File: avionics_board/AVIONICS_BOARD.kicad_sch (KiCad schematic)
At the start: 4 parts

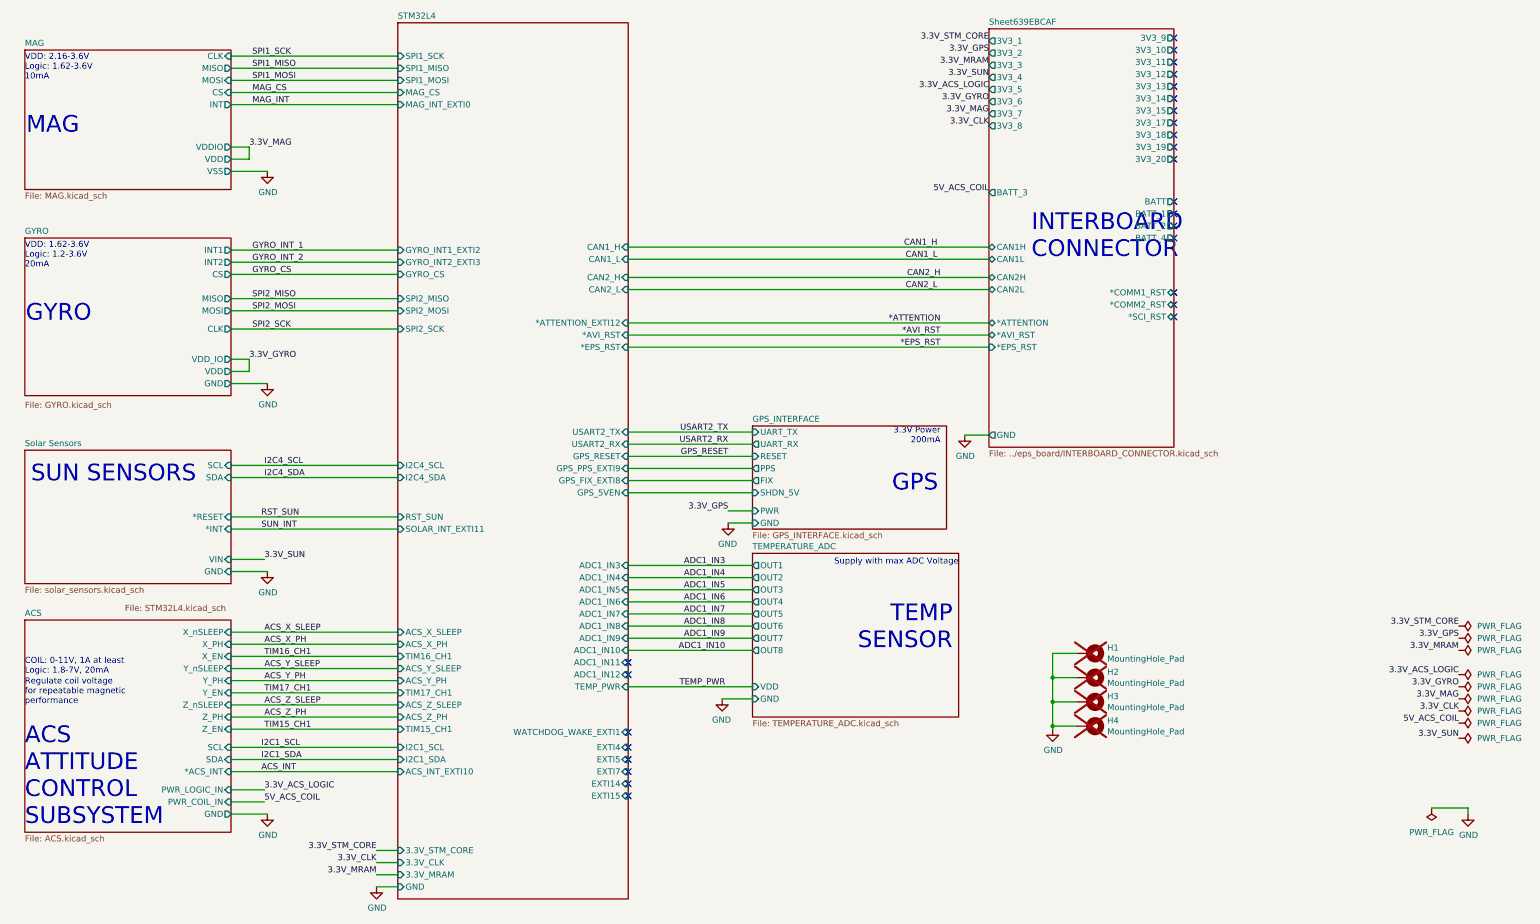
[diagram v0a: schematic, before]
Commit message: QC, add second 3V regulator to AUX, INT pullups on AUX SCI AVI
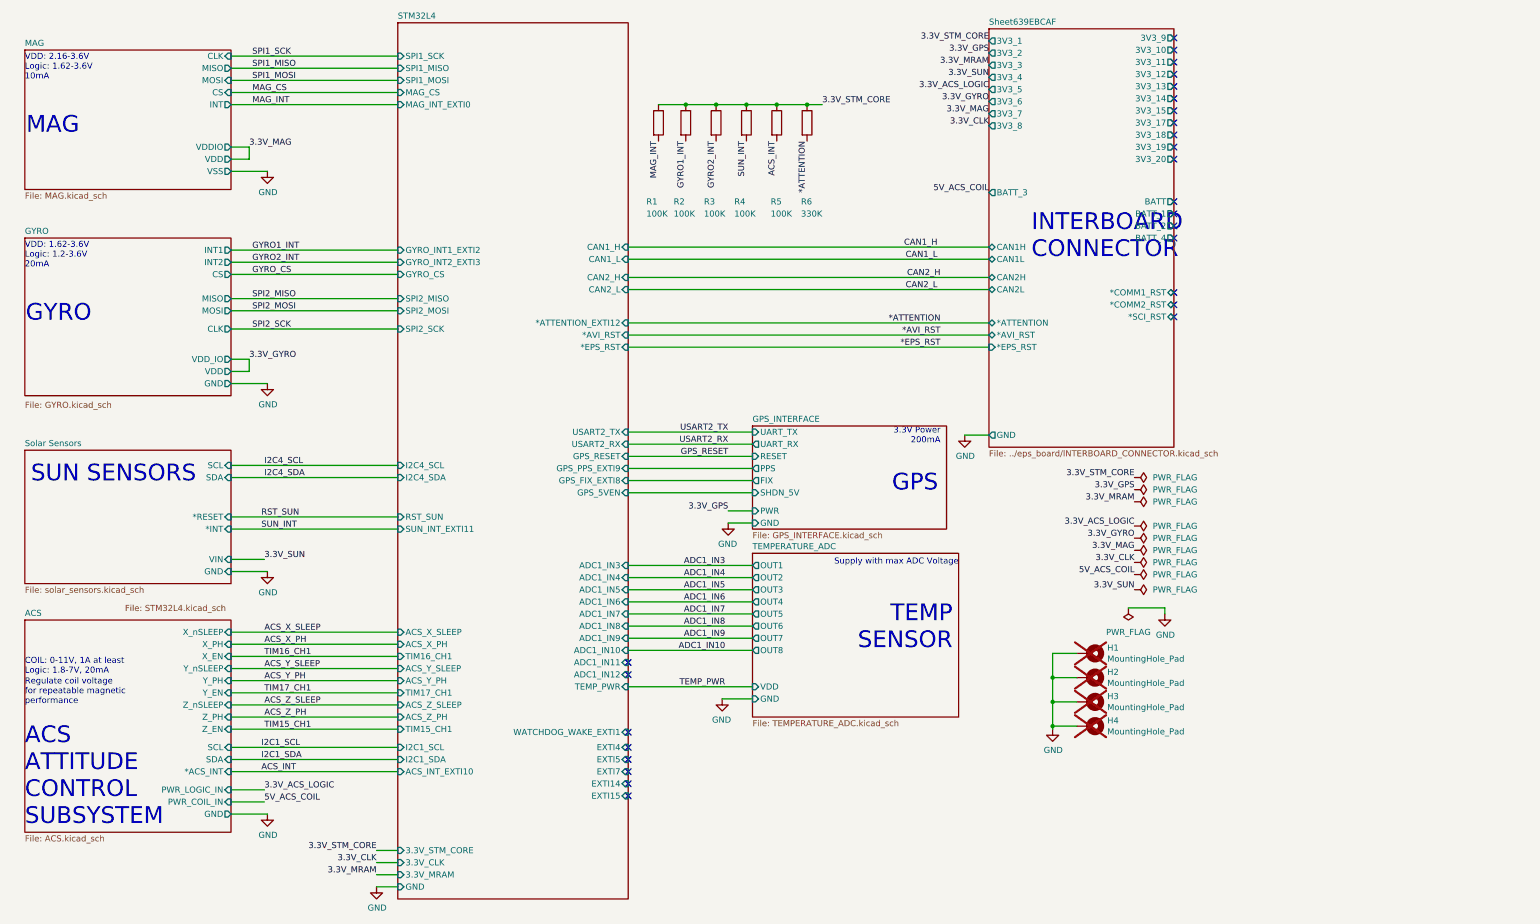
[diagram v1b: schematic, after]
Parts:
- added R1, R2, R3, R4, R5: 100K, Resistor_SMD:R_0402_1005Metric_Pad0.72x0.64mm_HandSolder, symbol Device:R
- added R6: 330K, Resistor_SMD:R_0402_1005Metric_Pad0.72x0.64mm_HandSolder, symbol Device:R
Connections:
- net *ATTENTION: now also R6.2
- net 3.3V_STM_CORE: now also R1.1, R2.1, R3.1, R4.1, R5.1, R6.1
- net ACS_INT: now also R5.2
- net MAG_INT: now also R1.2
- net SUN_INT: now also R4.2
- new net GYRO1_INT: R2.2
- new net GYRO2_INT: R3.2
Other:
- sheet STM32L4 ports: added SUN_INT_EXTI11; removed SOLAR_INT_EXTI11

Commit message: AVI board manages its local powers
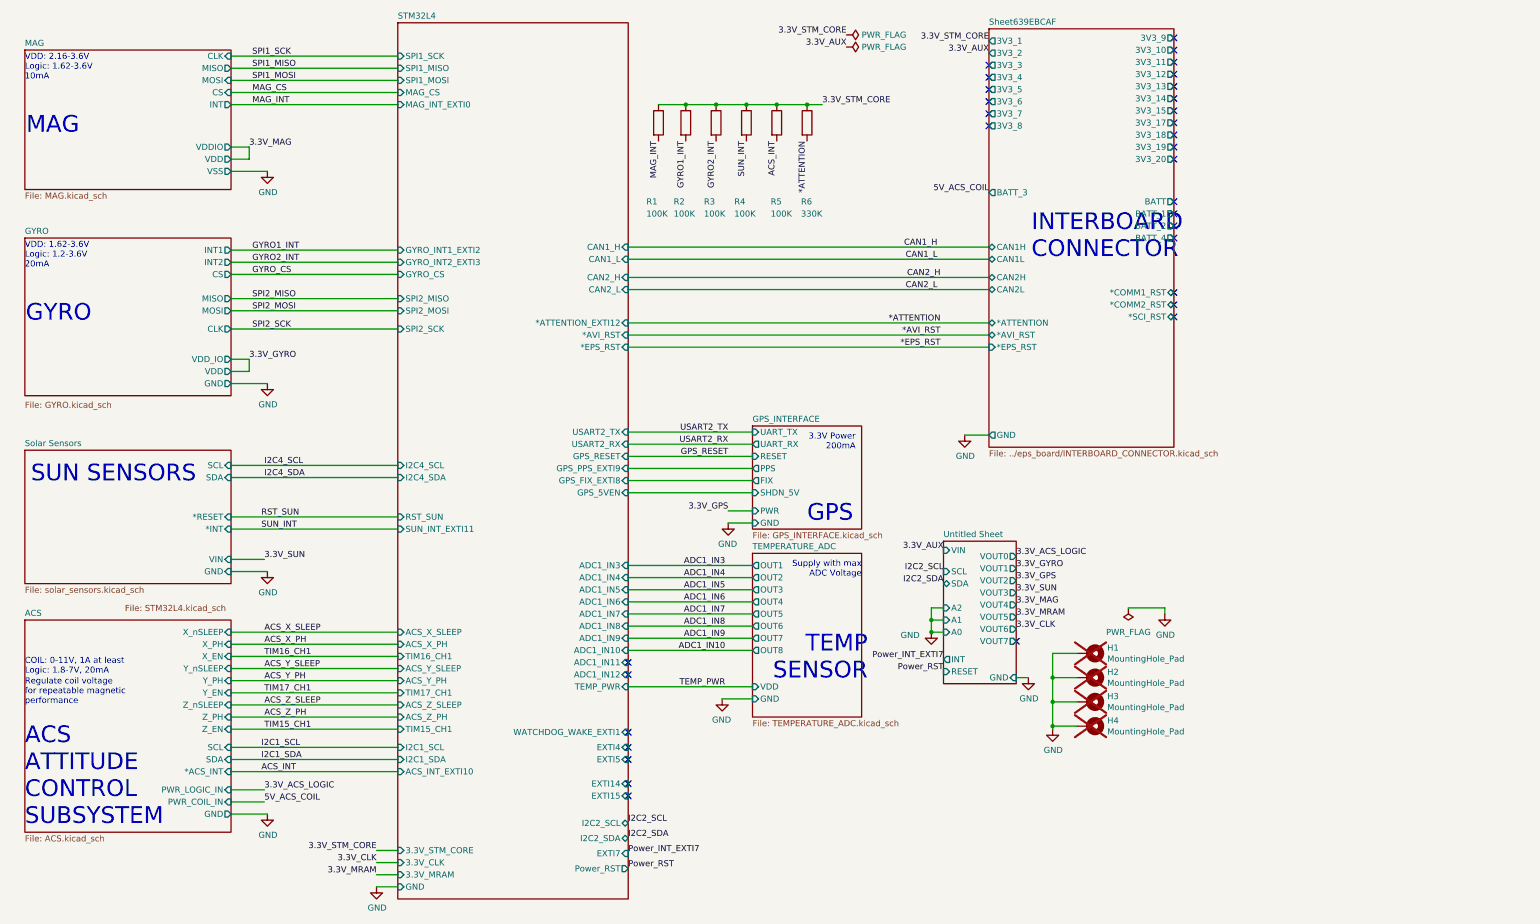
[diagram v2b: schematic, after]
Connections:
- no-connect marks 26 -> 32
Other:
- added sheet Untitled Sheet (../eps_board/i2c_power_switches_3v_sch.kicad_sch)
- sheet STM32L4 ports: added I2C2_SCL, I2C2_SDA, Power_RST; removed none
